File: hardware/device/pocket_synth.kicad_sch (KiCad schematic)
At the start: 0 parts

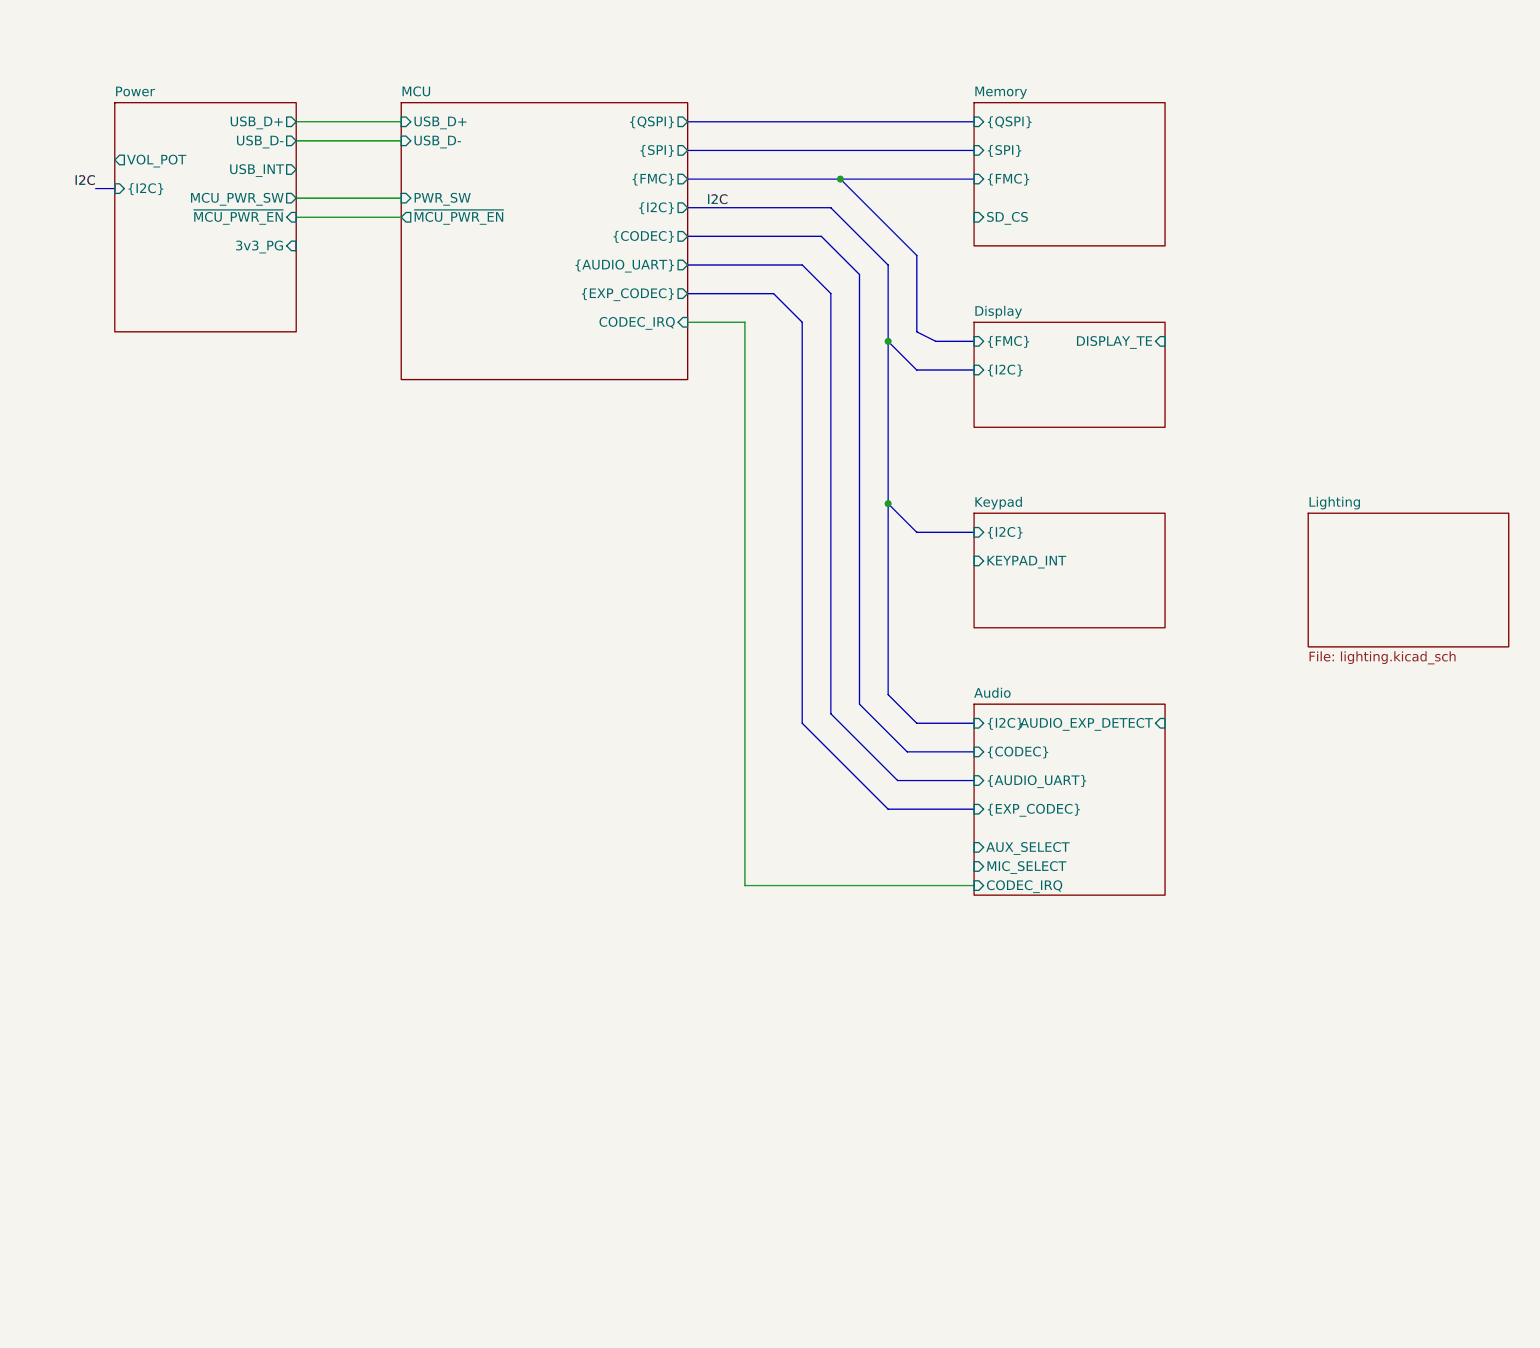
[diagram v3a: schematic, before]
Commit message: feat: add plated mounting holes
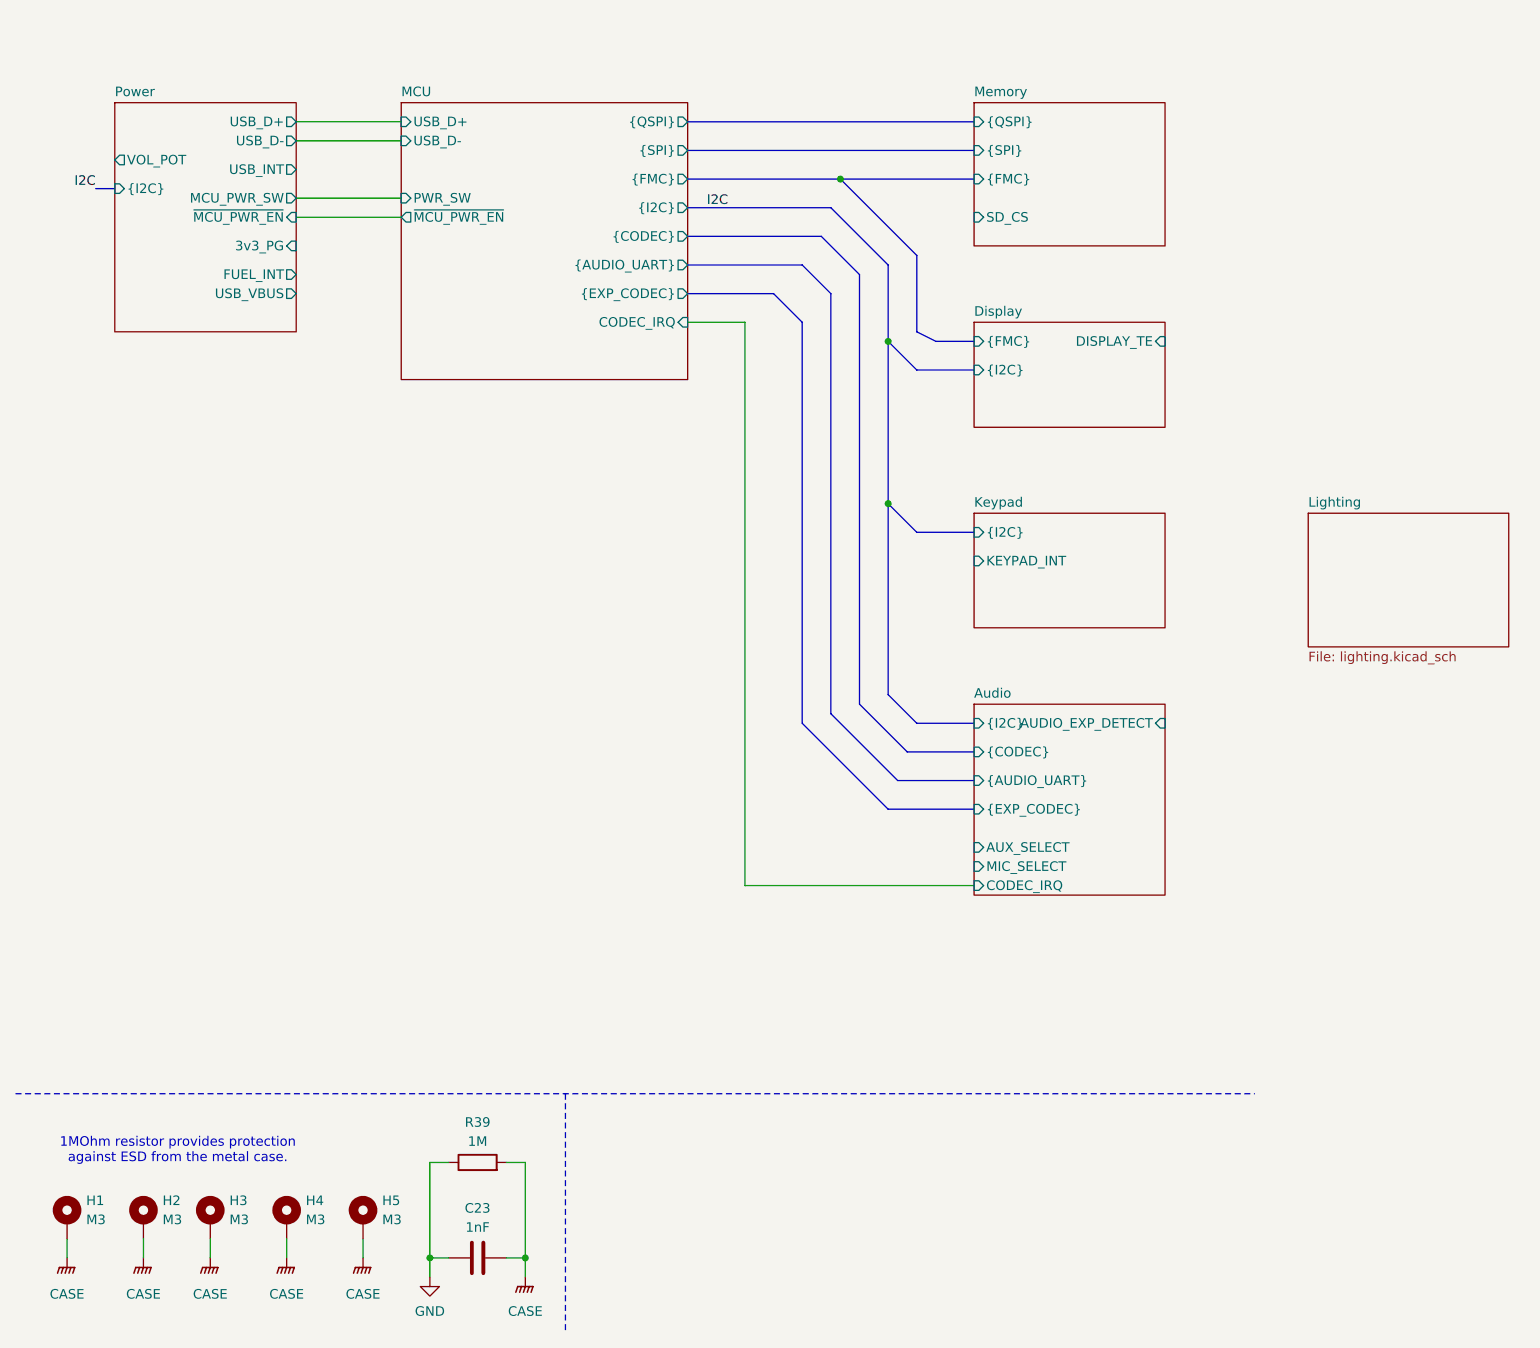
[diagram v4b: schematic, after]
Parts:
- added C23: 1nF, symbol Device:C
- added H1, H2, H3, H4, H5: M3, MountingHole:MountingHole_3.2mm_M3_DIN965_Pad, symbol Mechanical:MountingHole_Pad
- added R39: 1M, symbol Device:R
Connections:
- new net CASE: C23.2, H1.1, H2.1, H3.1, H4.1, H5.1, R39.2
- new net GND: C23.1, R39.1
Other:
- sheet Power ports: added FUEL_INT, USB_VBUS; removed none
- note added: "1MOhm resistor provides protection against ESD from the metal case."

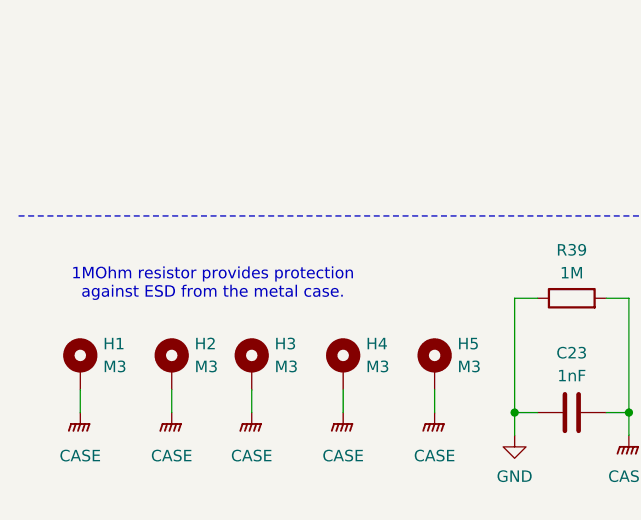
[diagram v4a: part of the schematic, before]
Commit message: feat: start routing keyswitch pads
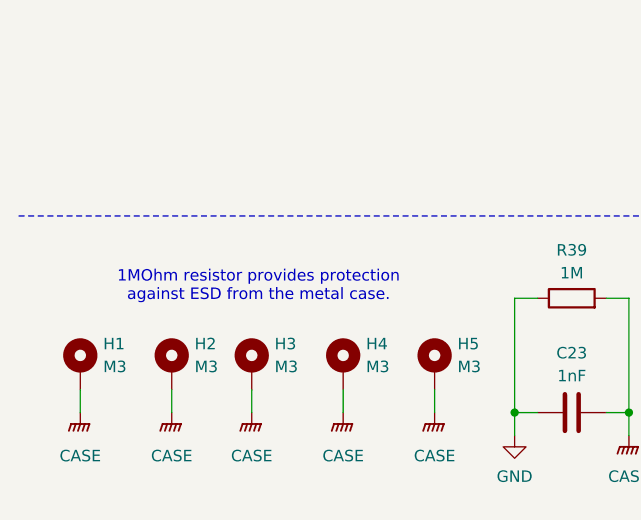
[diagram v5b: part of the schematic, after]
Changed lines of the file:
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@@
 	(text "1MOhm resistor provides protection\nagainst ESD from the metal case."
 		(exclude_from_sim no)
-		(at 33.782 171.958 0)
+		(at 38.862 172.212 0)
 		(effects
 			(font

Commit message: feat: audio system routing
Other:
- sheet Audio ports: added none; removed AUX_SELECT
- sheet MCU ports: added MIC_SELECT; removed none
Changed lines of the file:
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@@
+		)
+	)
+	(wire
+		(pts
+			(xy 106.68 134.62) (xy 139.7 134.62)
+		)
+		(stroke
+			(width 0)
+			(type default)
 		)
 	)
@@
 	(wire
 		(pts
-			(xy 109.22 63.5) (xy 109.22 138.43)
+			(xy 109.22 63.5) (xy 109.22 132.08)
 		)
 		(stroke
@@
 		)
 	)
+	(wire
+		(pts
+			(xy 101.6 66.04) (xy 106.68 66.04)
+		)
+		(stroke
+			(width 0)
+			(type default)
+		)
+	)
 	(bus
 		(pts
@@
 		(pts
 			(xy 101.6 59.69) (xy 113.03 59.69)
+		)
+		(stroke
+			(width 0)
+			(type default)
+		)
+	)
+	(wire
+		(pts
+			(xy 106.68 66.04) (xy 106.68 134.62)
 		)
 		(stroke
@@
 	(wire
 		(pts
-			(xy 109.22 138.43) (xy 139.7 138.43)
+			(xy 109.22 132.08) (xy 139.7 132.08)
 		)
 		(stroke
@@
 		)
 	)
-	(label "I2C"
+	(label "{I2C}"
 		(at 22.86 45.72 180)
 		(effects
@@
 		)
 	)
-	(label "I2C"
+	(label "{I2C}"
 		(at 104.14 48.26 0)
 		(effects
@@
 			)
 		)
+		(pin "MIC_SELECT" output
+			(at 101.6 66.04 0)
+			(effects
+				(font
+					(size 1.27 1.27)
+				)
+				(justify right)
+			)
+		)
 		(instances
 			(project "pocket_synth"
@@
 	(sheet
 		(at 139.7 114.3)
-		(size 25.4 25.4)
+		(size 25.4 26.67)
 		(exclude_from_sim no)
 		(in_bom yes)
@@
 		)
 		(property "Sheetfile" "audio.kicad_sch"
-			(at 139.7 140.2846 0)
+			(at 139.7 141.5546 0)
 			(effects
 				(font
@@
 			)
 		)
-		(pin "CODEC_IRQ" input
-			(at 139.7 138.43 180)
+		(pin "CODEC_IRQ" output
+			(at 139.7 132.08 180)
 			(effects
 				(font
@@
 			)
 		)
-		(pin "AUX_SELECT" input
-			(at 139.7 133.35 180)
-			(effects
-				(font
-					(size 1.27 1.27)
-				)
-				(justify left)
-			)
-		)
 		(pin "MIC_SELECT" input
-			(at 139.7 135.89 180)
-			(effects
-				(font
+			(at 139.7 134.62 180)
+			(effects
+				(font
